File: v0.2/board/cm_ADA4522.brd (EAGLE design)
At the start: 75.2 x 52.7 mm, 105 parts, among them J1 10118194-0001LF, U1 ADA4522-4ARZ

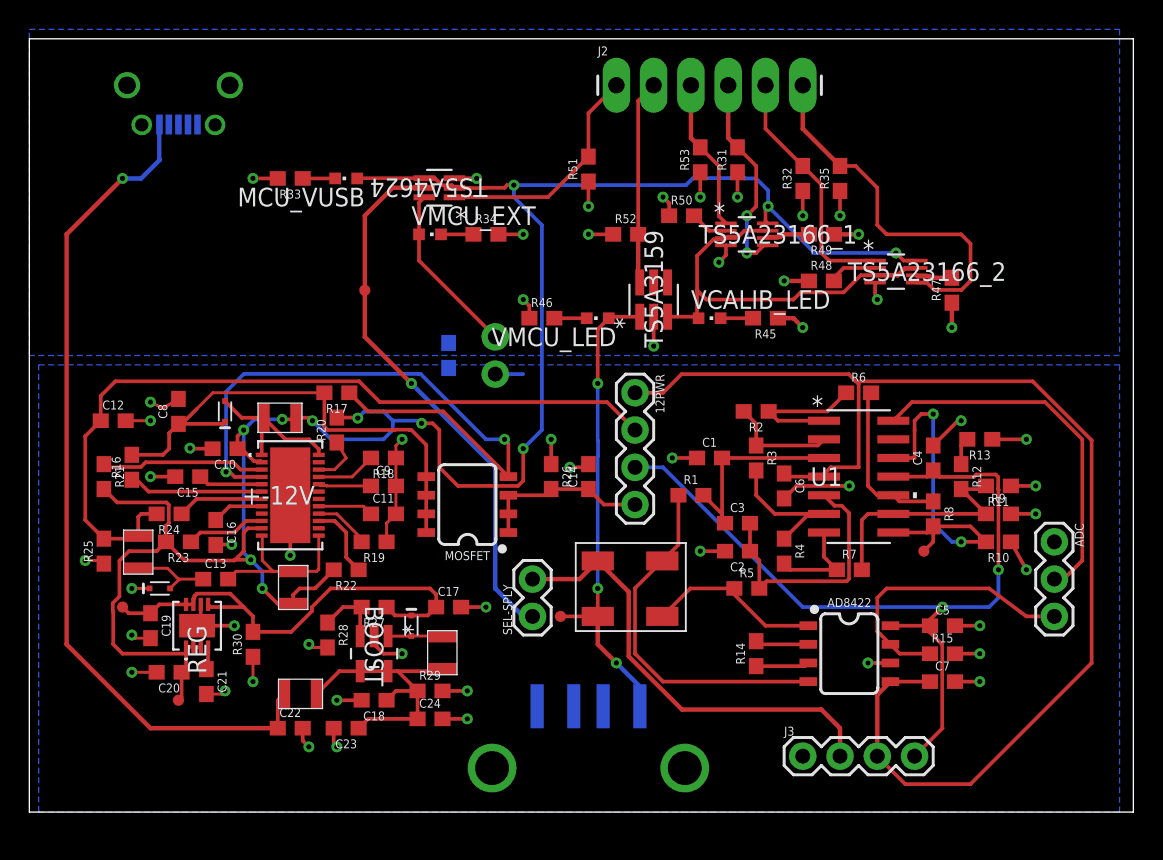
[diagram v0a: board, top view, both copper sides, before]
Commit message: connect data ports from usb
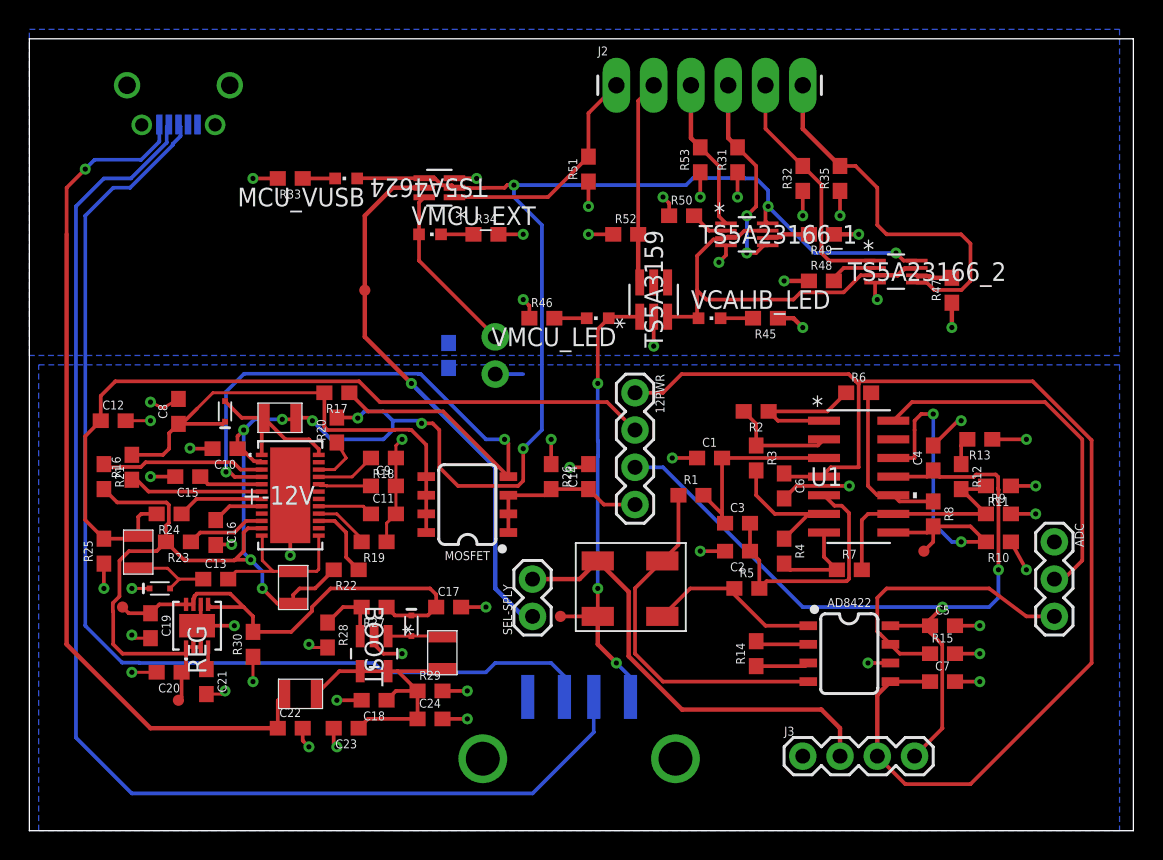
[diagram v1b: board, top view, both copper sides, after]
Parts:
- moved MCU 0.90 mm to (35.6, 0.64)
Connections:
- removed net D+: J1.3
- removed net D-: J1.2
- new net DATA+: J1.3, MCU.D+
- new net DATA-: J1.2, MCU.D-
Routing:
- net DATA-: track 0.00 -> 86.5 mm
- net DATA+: track 0.00 -> 73.6 mm
- net 5VIN: track 58.1 -> 59.2 mm
- net VSS: track 32.7 -> 31.8 mm
- net GND: track 76.4 -> 77.0 mm
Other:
- board size 75.2 x 52.7 mm -> 75.2 x 54 mm

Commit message: add names to external connectors
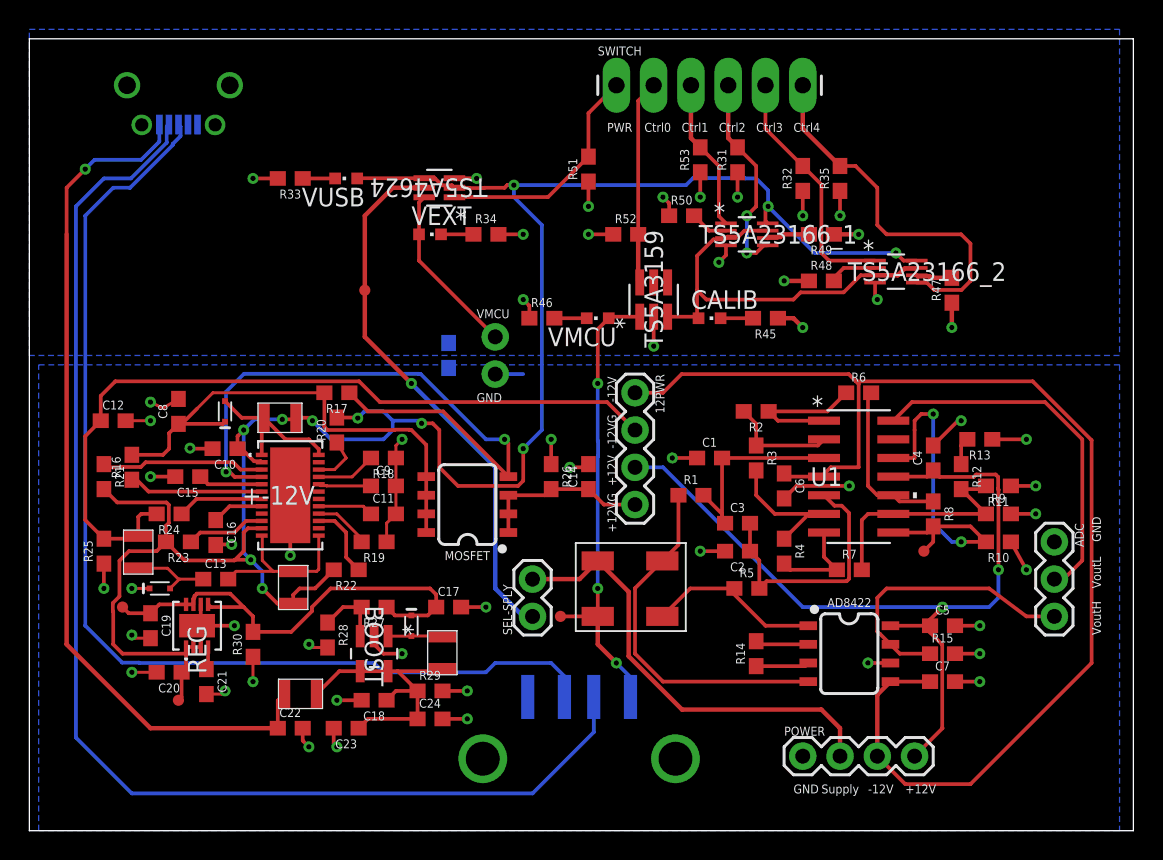
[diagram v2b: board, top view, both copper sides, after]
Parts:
- renumbered J1 to USB-IN, J2 to SWITCH, J3 to POWER, MCU to USB-OUT, MCU_VUSB to VUSB, VCALIB_LED to CALIB, VMCU_EXT to VEXT, VMCU_LED to VMCU
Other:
- board text added: "+12V"
- board text added: "+12VG"
- board text added: "-12V"
- board text added: "-12VG"
- board text added: "Ctrl0"
- board text added: "Ctrl1"
- board text added: "Ctrl2"
- board text added: "Ctrl3"
- board text added: "Ctrl4"
- board text added: "GND"
- board text added: "PWR"
- board text added: "Supply"
- board text added: "VMCU"
- board text added: "VoutH"
- board text added: "VoutL"
